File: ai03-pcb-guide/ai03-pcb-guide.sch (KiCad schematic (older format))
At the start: 24 parts, among them SW1 SW_Push, U1 ATmega32U4-AU, Y1 16MHz

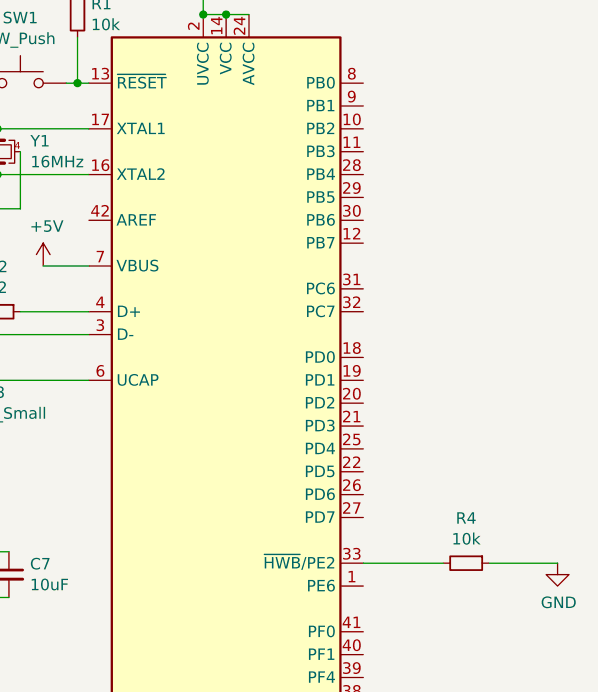
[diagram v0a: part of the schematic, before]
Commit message: routed
moved around components and routed wires
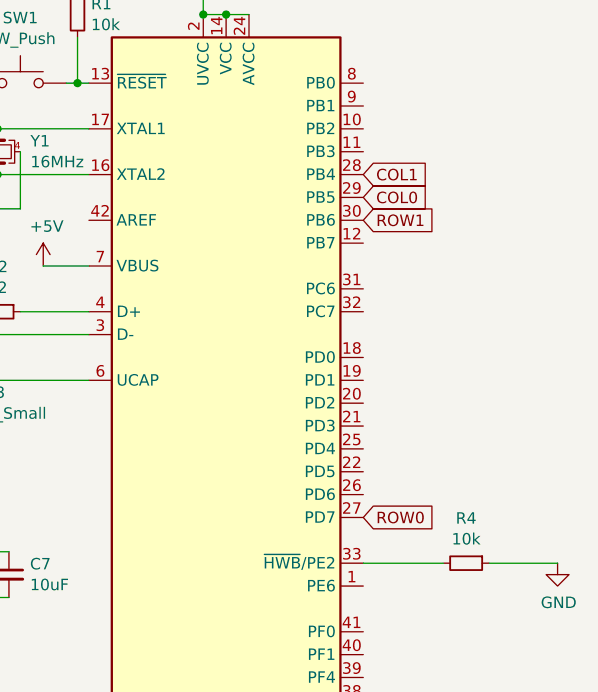
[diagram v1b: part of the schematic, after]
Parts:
- MX1, MX2: footprint Fuse:Fuse_1206_3216Metric -> MX_Alps_Hybrid:MX-1U-NoLED
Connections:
- net COL0: now also U1.29 (PB5)
- net COL1: now also U1.28 (PB4)
- net ROW0: now also U1.27 (PD7)
- net ROW1: now also U1.30 (PB6)
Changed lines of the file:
@@
 F 0 "MX2" H 2783 1573 60  0000 C CNN
 F 1 "MX-NoLED" H 2783 1499 20  0000 C CNN
-F 2 "Fuse:Fuse_1206_3216Metric" H 2125 1325 60  0001 C CNN
+F 2 "MX_Alps_Hybrid:MX-1U-NoLED" H 2125 1325 60  0001 C CNN
 F 3 "" H 2125 1325 60  0001 C CNN
 	1    2750 1350
@@
 F 0 "MX1" H 2133 1573 60  0000 C CNN
 F 1 "MX-NoLED" H 2133 1499 20  0000 C CNN
-F 2 "Fuse:Fuse_1206_3216Metric" H 1475 1325 60  0001 C CNN
+F 2 "MX_Alps_Hybrid:MX-1U-NoLED" H 1475 1325 60  0001 C CNN
 F 3 "" H 1475 1325 60  0001 C CNN
 	1    2100 1350
@@
 Text GLabel 1650 2550 0    50   Input ~ 0
 ROW1
+Text GLabel 6150 1650 2    50   Input ~ 0
+COL1
+Text GLabel 6150 1750 2    50   Input ~ 0
+COL0
+Text GLabel 6150 1850 2    50   Input ~ 0
+ROW1
+Text GLabel 6150 3150 2    50   Input ~ 0
+ROW0
 $EndSCHEMATC
